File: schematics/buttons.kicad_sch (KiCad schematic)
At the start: 0 parts

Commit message: Update
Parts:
- added VR1, VR2, VR3, VR4: PTL60-15G1-103B2, 00_Luc:PTL6015G1103B2, symbol 00_PTL60:PTL60-15G1-103B2

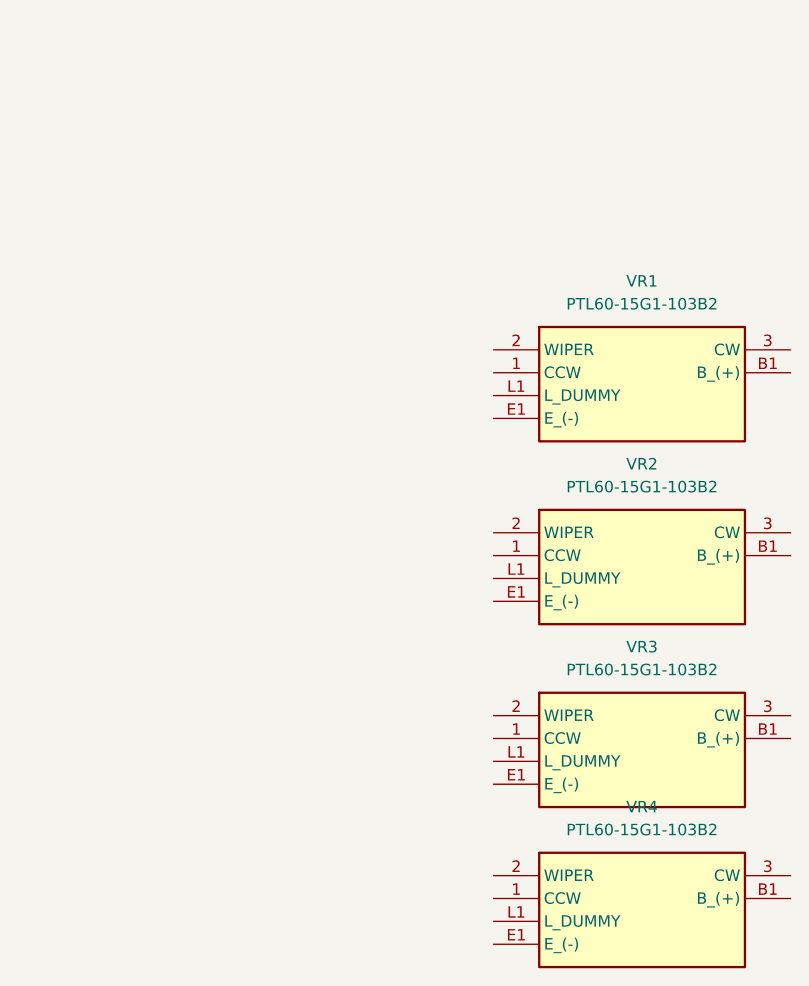
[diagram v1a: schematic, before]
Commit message: Introduce buttons and update pcb layout
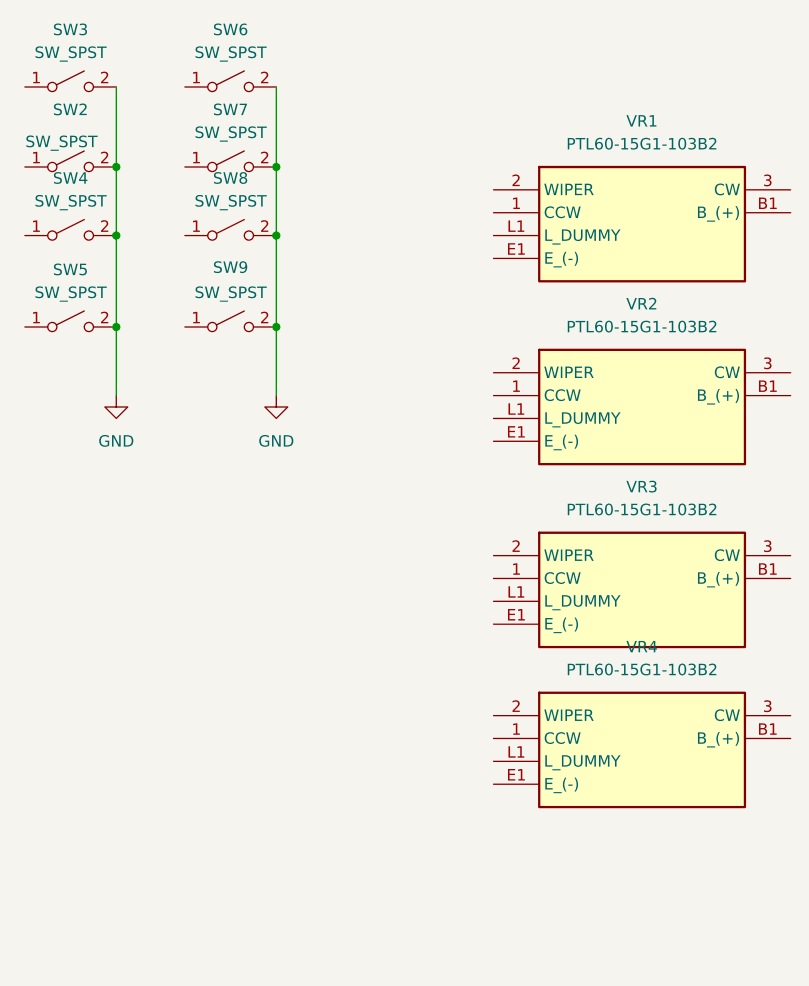
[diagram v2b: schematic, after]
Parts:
- added SW2, SW3, SW4, SW5, SW6, SW7, SW8, SW9: SW_SPST, PCM_Switch_Keyboard_Cherry_MX:SW_Cherry_MX_PCB_1.00u, symbol Switch:SW_SPST
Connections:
- new net GND: SW2.2 (B), SW3.2 (B), SW4.2 (B), SW5.2 (B), SW6.2 (B), SW7.2 (B), SW8.2 (B), SW9.2 (B)
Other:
- moved on the sheet: VR1, VR2, VR3, VR4

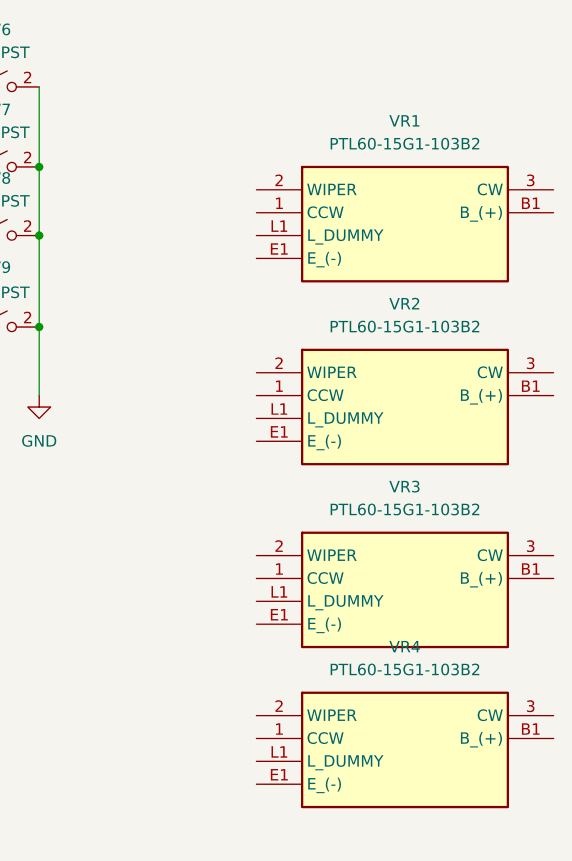
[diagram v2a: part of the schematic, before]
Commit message: Make square
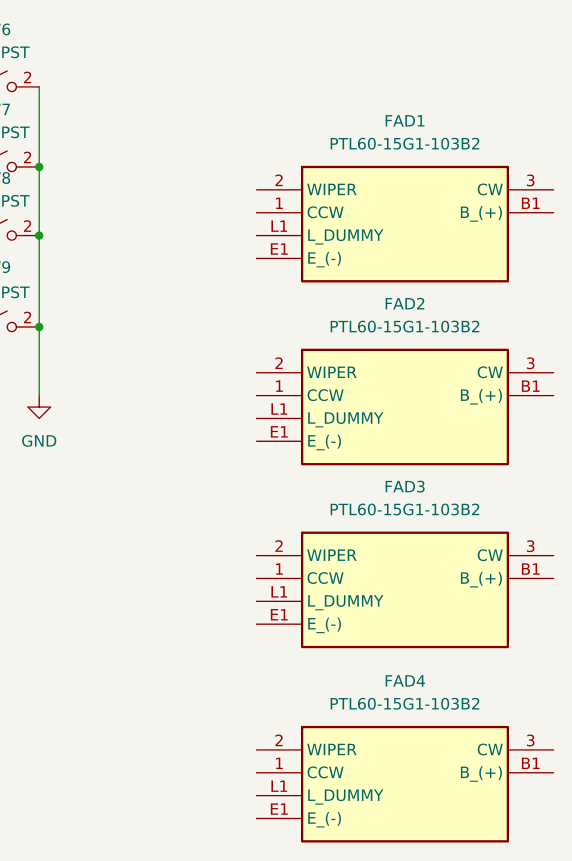
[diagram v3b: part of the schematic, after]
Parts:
- removed VR4: PTL60-15G1-103B2, 00_Luc:PTL6015G1103B2, symbol 00_PTL60:PTL60-15G1-103B2
- added FAD4: PTL60-15G1-103B2, 00_Luc:PTL6015G1103B2, symbol 00_PTL60:PTL60-15G1-103B2
- renumbered VR1 to FAD1, VR2 to FAD2, VR3 to FAD3
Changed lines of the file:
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@@
 		(dnp no)
 		(fields_autoplaced yes)
-		(property "Reference" "VR2"
+		(property "Reference" "FAD2"
 			(at 142.24 85.09 0)
 			(effects
@@
 			(project "miixer"
 				(path "/f2af4cd4-99cf-4d01-92f6-6413371e0fe3/5611f13c-04e1-436b-9132-43ac5c8df051"
-					(reference "VR2")
+					(reference "FAD2")
 					(unit 1)
 				)
@@
 		(dnp no)
 		(fields_autoplaced yes)
-		(property "Reference" "VR3"
+		(property "Reference" "FAD3"
 			(at 142.24 105.41 0)
 			(effects
@@
 			(project "miixer"
 				(path "/f2af4cd4-99cf-4d01-92f6-6413371e0fe3/5611f13c-04e1-436b-9132-43ac5c8df051"
-					(reference "VR3")
+					(reference "FAD3")
 					(unit 1)
 				)
@@
 	)
 	(symbol
+		(lib_id "00_PTL60:PTL60-15G1-103B2")
+		(at 125.73 134.62 0)
+		(unit 1)
+		(exclude_from_sim no)
+		(in_bom yes)
+		(on_board yes)
+		(dnp no)
+		(fields_autoplaced yes)
+		(property "Reference" "FAD4"
+			(at 142.24 127 0)
+			(effects
+				(font
+					(size 1.27 1.27)
+				)
+			)
+		)
+		(property "Value" "PTL60-15G1-103B2"
+			(at 142.24 129.54 0)
+			(effects
+				(font
+					(size 1.27 1.27)
+				)
+			)
+		)
+		(property "Footprint" "00_Luc:PTL6015G1103B2"
+			(at 154.94 229.54 0)
+			(effects
+				(font
+					(size 1.27 1.27)
+				)
+				(justify left top)
+				(hide yes)
+			)
+		)
+		(property "Datasheet" "https://www.bourns.com/docs/Product-Datasheets/PTL.pdf"
+			(at 154.94 329.54 0)
+			(effects
+				(font
+					(size 1.27 1.27)
+				)
+				(justify left top)
+				(hide yes)
+			)
+		)
+		(property "Description" "Bourns 1 Gang Slide Carbon Potentiometer with an 6 mm Dia. Shaft - 10k, +/-20%, 0.2W Power Rating, Linear, Through Hole"
+			(at 125.73 134.62 0)
+			(effects
+				(font
+					(size 1.27 1.27)
+				)
+				(hide yes)
+			)
+		)
+		(property "Height" "22"
+			(at 154.94 529.54 0)
+			(effects
+				(font
+					(size 1.27 1.27)
+				)
+				(justify left top)
+				(hide yes)
+			)
+		)
+		(property "Mouser Part Number" "652-PTL60-15G1-103B2"
+			(at 154.94 629.54 0)
+			(effects
+				(font
+					(size 1.27 1.27)
+				)
+				(justify left top)
+				(hide yes)
+			)
+		)
+		(property "Mouser Price/Stock" "https://www.mouser.co.uk/ProductDetail/Bourns/PTL60-15G1-103B2?qs=XxajcJZMfNxADct0M%2FB1oA%3D%3D"
+			(at 154.94 729.54 0)
+			(effects
+				(font
+					(size 1.27 1.27)
+				)
+				(justify left top)
+				(hide yes)
+			)
+		)
+		(property "Manufacturer_Name" "Bourns"
+			(at 154.94 829.54 0)
+			(effects
+				(font
+					(size 1.27 1.27)
+				)
+				(justify left top)
+				(hide yes)
+			)
+		)
+		(property "Manufacturer_Part_Number" "PTL60-15G1-103B2"
+			(at 154.94 929.54 0)
+			(effects
+				(font
+					(size 1.27 1.27)
+				)
+				(justify left top)
+				(hide yes)
+			)
+		)
+		(pin "3"
+		)
+		(pin "B1"
+		)
+		(pin "E1"
+		)
+		(pin "2"
+		)
+		(pin "L1"
+		)
+		(pin "1"
+		)
+		(instances
+			(project "miixer"
+				(path "/f2af4cd4-99cf-4d01-92f6-6413371e0fe3/5611f13c-04e1-436b-9132-43ac5c8df051"
+					(reference "FAD4")
+					(unit 1)
+				)
+			)
+		)
+	)
+	(symbol
 		(lib_id "power:GND")
 		(at 83.82 95.25 0)
@@
 	)
 	(symbol
-		(lib_id "00_PTL60:PTL60-15G1-103B2")
-		(at 125.73 130.81 0)
-		(unit 1)
-		(exclude_from_sim no)
-		(in_bom yes)
-		(on_board yes)
-		(dnp no)
-		(fields_autoplaced yes)
-		(property "Reference" "VR4"
-			(at 142.24 123.19 0)
-			(effects
-				(font
-					(size 1.27 1.27)
-				)
-			)
-		)
-		(property "Value" "PTL60-15G1-103B2"
-			(at 142.24 125.73 0)
-			(effects
-				(font
-					(size 1.27 1.27)
-				)
-			)
-		)
-		(property "Footprint" "00_Luc:PTL6015G1103B2"
-			(at 154.94 225.73 0)
-			(effects
-				(font
-					(size 1.27 1.27)
-				)
-				(justify left top)
-				(hide yes)
-			)
-		)
-		(property "Datasheet" "https://www.bourns.com/docs/Product-Datasheets/PTL.pdf"
-			(at 154.94 325.73 0)
-			(effects
-				(font
-					(size 1.27 1.27)
-				)
-				(justify left top)
-				(hide yes)
-			)
-		)
-		(property "Description" "Bourns 1 Gang Slide Carbon Potentiometer with an 6 mm Dia. Shaft - 10k, +/-20%, 0.2W Power Rating, Linear, Through Hole"
-			(at 125.73 130.81 0)
-			(effects
-				(font
-					(size 1.27 1.27)
-				)
-				(hide yes)
-			)
-		)
-		(property "Height" "22"
-			(at 154.94 525.73 0)
-			(effects
-				(font
-					(size 1.27 1.27)
-				)
-				(justify left top)
-				(hide yes)
-			)
-		)
-		(property "Mouser Part Number" "652-PTL60-15G1-103B2"
-			(at 154.94 625.73 0)
-			(effects
-				(font
-					(size 1.27 1.27)
-				)
-				(justify left top)
-				(hide yes)
-			)
-		)
-		(property "Mouser Price/Stock" "https://www.mouser.co.uk/ProductDetail/Bourns/PTL60-15G1-103B2?qs=XxajcJZMfNxADct0M%2FB1oA%3D%3D"
-			(at 154.94 725.73 0)
-			(effects
-				(font
-					(size 1.27 1.27)
-				)
-				(justify left top)
-				(hide yes)
-			)
-		)
-		(property "Manufacturer_Name" "Bourns"
-			(at 154.94 825.73 0)
-			(effects
-				(font
-					(size 1.27 1.27)
-				)
-				(justify left top)
-				(hide yes)
-			)
-		)
-		(property "Manufacturer_Part_Number" "PTL60-15G1-103B2"
-			(at 154.94 925.73 0)
-			(effects
-				(font
-					(size 1.27 1.27)
-				)
-				(justify left top)
-				(hide yes)
-			)
-		)
-		(pin "3"
-		)
-		(pin "B1"
-		)
-		(pin "E1"
-		)
-		(pin "2"
-		)
-		(pin "L1"
-		)
-		(pin "1"
-		)
-		(instances
-			(project "miixer"
-				(path "/f2af4cd4-99cf-4d01-92f6-6413371e0fe3/5611f13c-04e1-436b-9132-43ac5c8df051"
-					(reference "VR4")
-					(unit 1)
-				)
-			)
-		)
-	)
-	(symbol
 		(lib_id "Switch:SW_SPST")
 		(at 96.52 77.47 0)
@@
 		(dnp no)
 		(fields_autoplaced yes)
-		(property "Reference" "VR1"
+		(property "Reference" "FAD1"
 			(at 142.24 64.77 0)
 			(effects
@@
 			(project ""
 				(path "/f2af4cd4-99cf-4d01-92f6-6413371e0fe3/5611f13c-04e1-436b-9132-43ac5c8df051"
-					(reference "VR1")
-					(unit 1)
-				)
+					(reference "FAD1")
+					(unit 1)
+				)

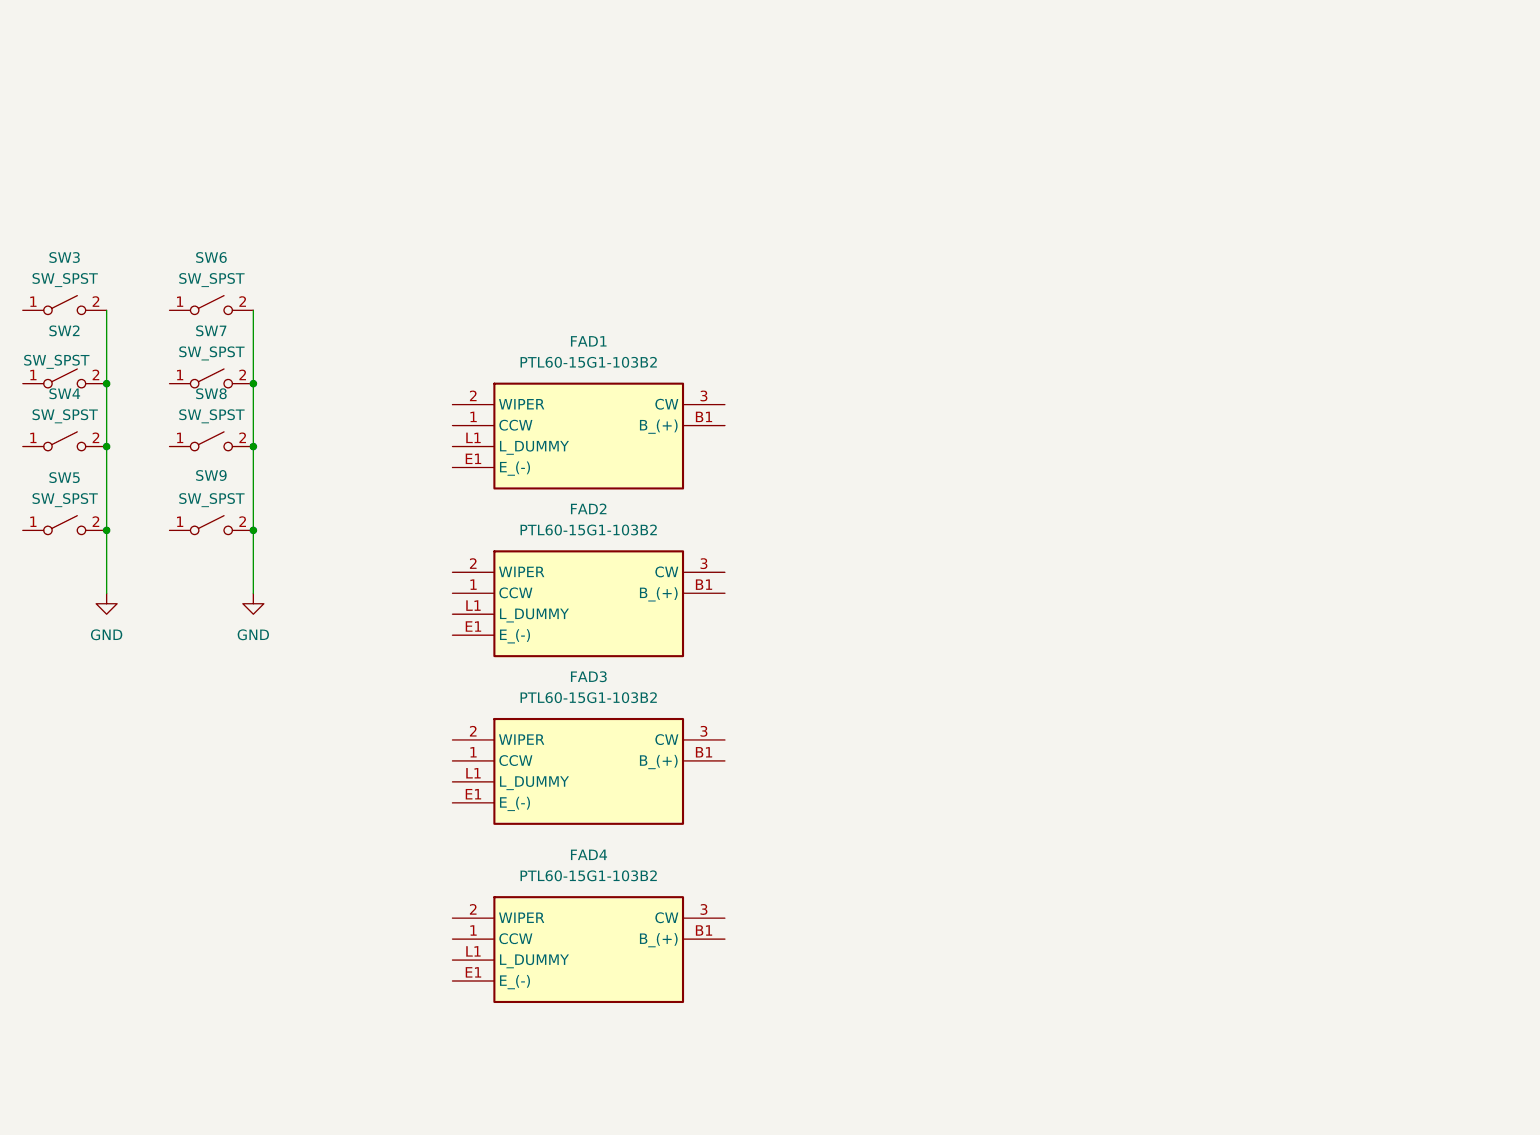
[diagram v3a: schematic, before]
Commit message: Add keys for each fader & update layout
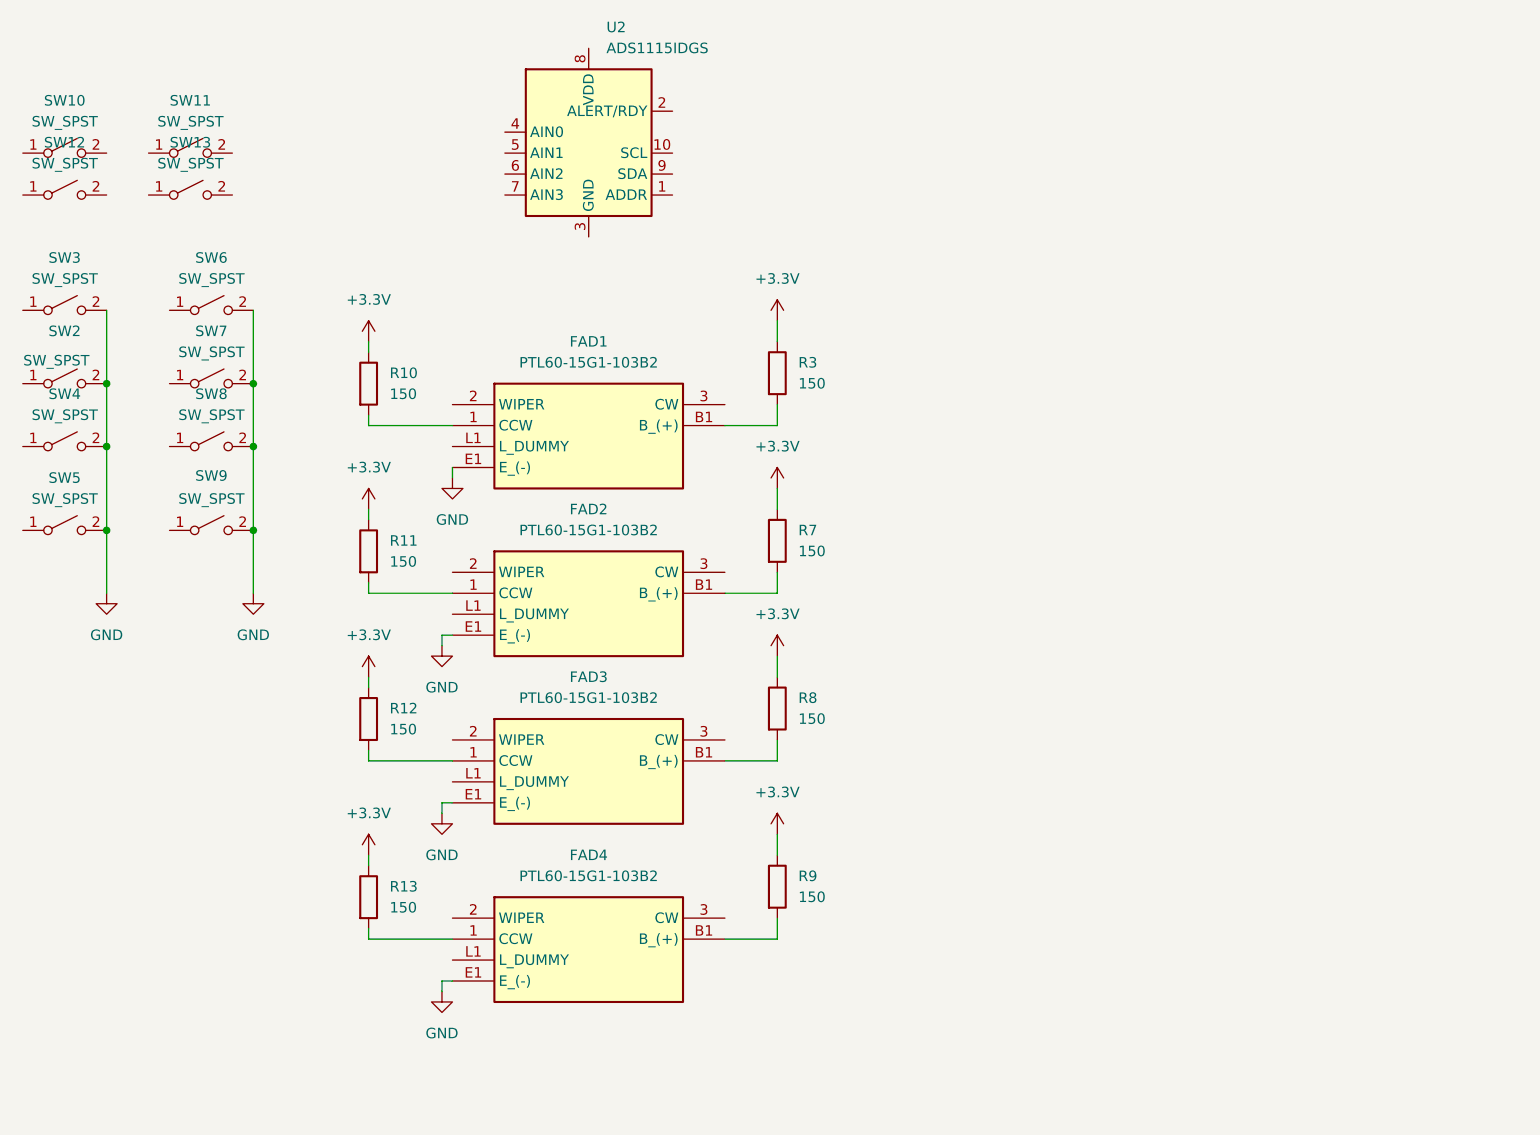
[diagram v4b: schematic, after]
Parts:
- added R10, R11, R12, R13, R3, R7, R8, R9: 150, symbol Device:R
- added SW10, SW11, SW12, SW13: SW_SPST, PCM_Switch_Keyboard_Cherry_MX:SW_Cherry_MX_PCB_1.00u, symbol Switch:SW_SPST
- added U2: ADS1115IDGS, Package_SO:TSSOP-10_3x3mm_P0.5mm, symbol Analog_ADC:ADS1115IDGS
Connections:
- net GND: now also FAD1.E1 (E_(-)), FAD2.E1 (E_(-)), FAD3.E1 (E_(-)), FAD4.E1 (E_(-))
- net at FAD2.1 (CCW): now also R11.2
- net at FAD2.B1 (B_(+)): now also R7.2
- net at FAD3.1 (CCW): now also R12.2
- net at FAD3.B1 (B_(+)): now also R8.2
- net at FAD4.1 (CCW): now also R13.2
- net at FAD4.B1 (B_(+)): now also R9.2
- net at FAD1.1 (CCW): now also R10.2
- net at FAD1.B1 (B_(+)): now also R3.2
- new net +3.3V: R10.1, R11.1, R12.1, R13.1, R3.1, R7.1, R8.1, R9.1

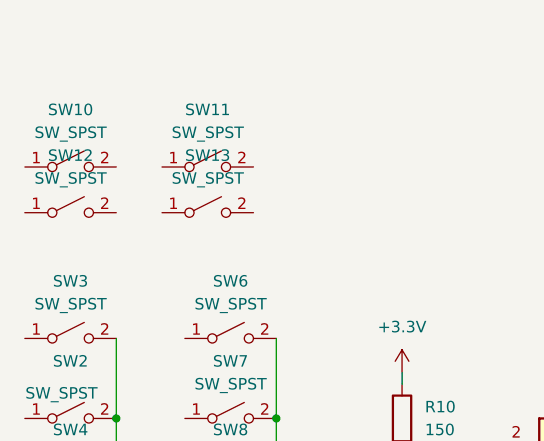
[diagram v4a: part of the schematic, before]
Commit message: Reorg layout and remove fader keys
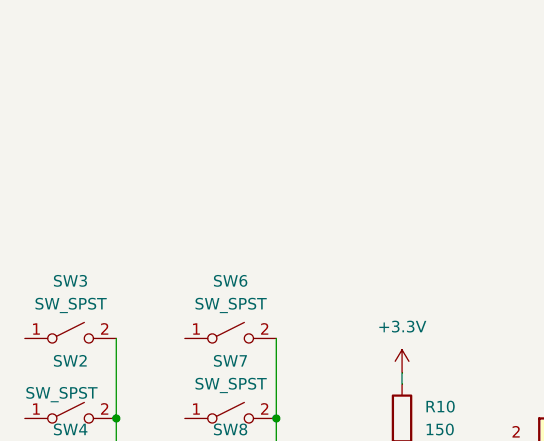
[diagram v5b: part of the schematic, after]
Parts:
- removed SW10, SW11, SW12, SW13: SW_SPST, PCM_Switch_Keyboard_Cherry_MX:SW_Cherry_MX_PCB_1.00u, symbol Switch:SW_SPST
